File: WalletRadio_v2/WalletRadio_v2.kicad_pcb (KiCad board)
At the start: 2 copper layers, 93.9 x 64 mm, 33 parts, among them Q1 BSP315P, Q2 Q_NPN_ECB, SW1 SW_SPDT, U1 BB201, U2 BB201, U3 LM324A

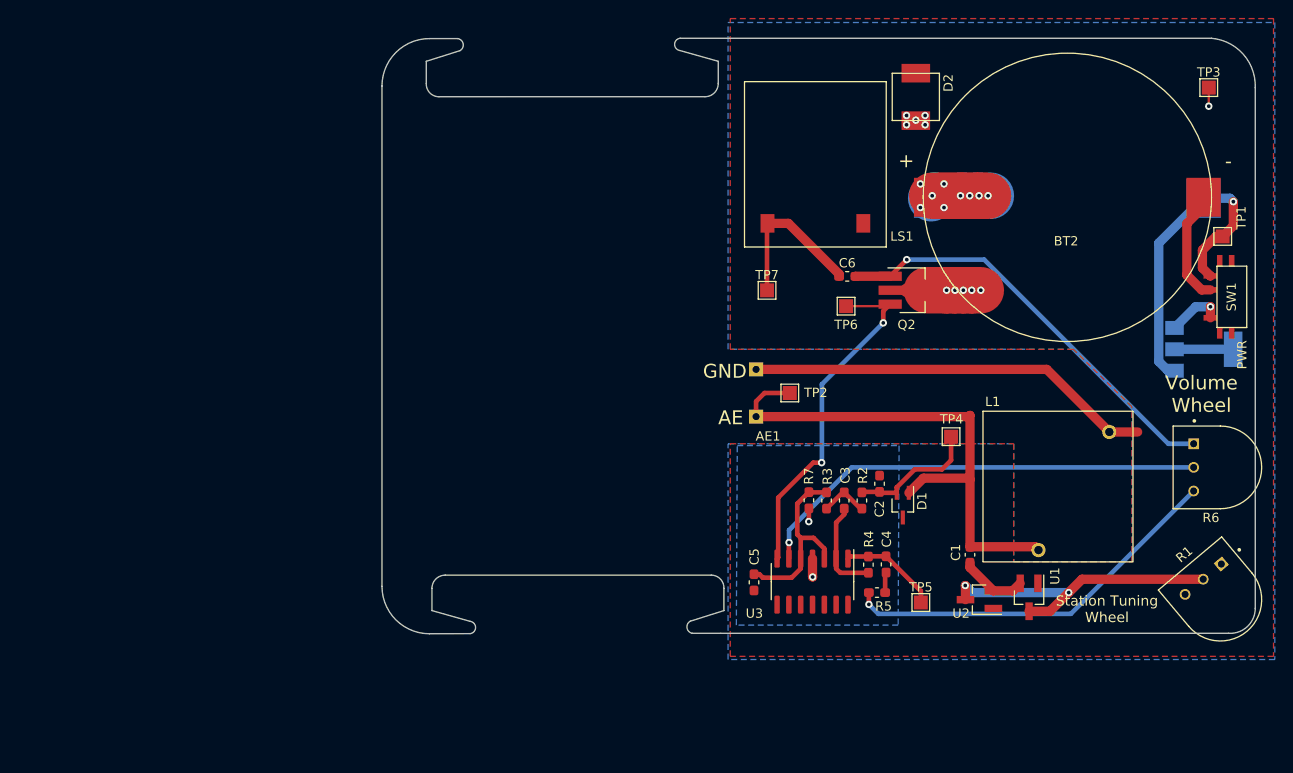
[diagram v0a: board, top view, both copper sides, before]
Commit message: Changed the coin cell holder. Redid entire PCB layout
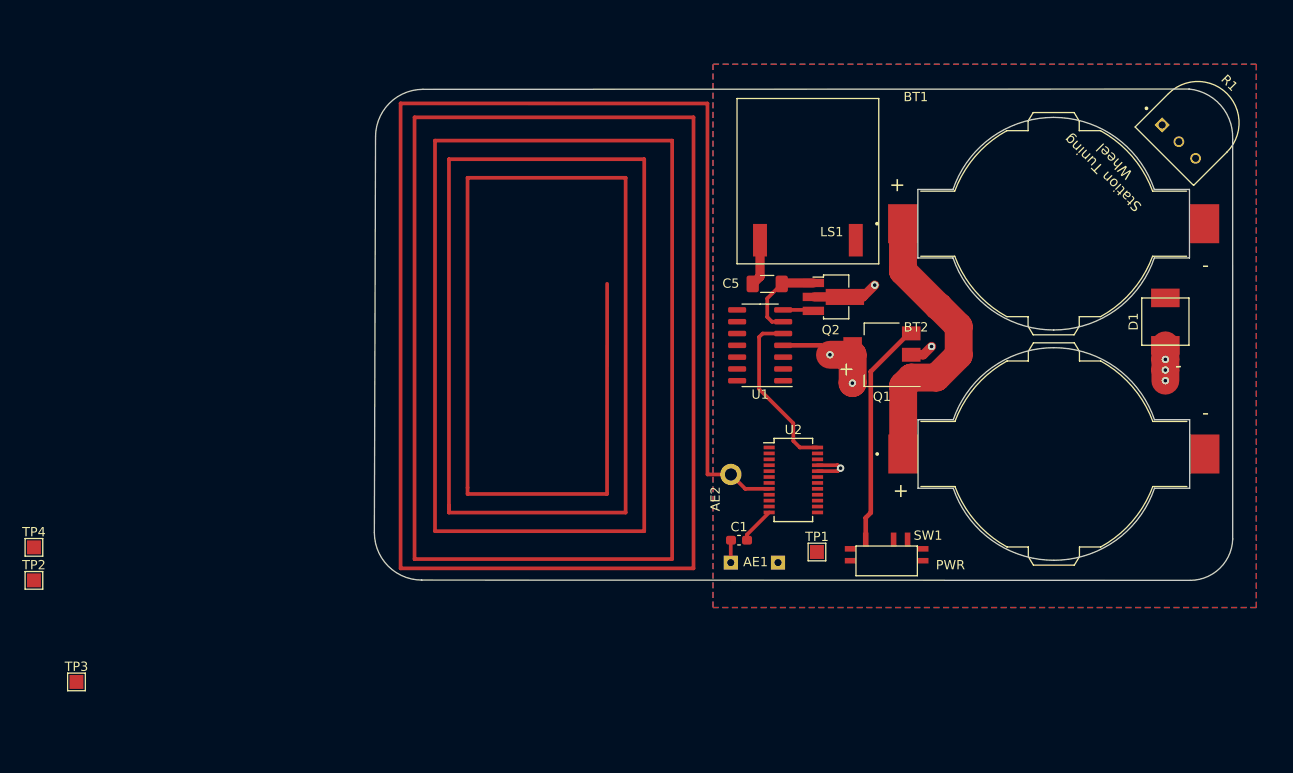
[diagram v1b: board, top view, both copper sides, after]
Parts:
- removed C2: 300pF, Capacitor_SMD:C_0603_1608Metric_Pad1.05x0.95mm_HandSolder
- removed C3: 0.1uF, Capacitor_SMD:C_0603_1608Metric_Pad1.05x0.95mm_HandSolder
- removed C4: 0.47uF, Capacitor_SMD:C_0603_1608Metric_Pad1.05x0.95mm_HandSolder
- removed C6: 100uF, Resistor_SMD:R_0603_1608Metric_Pad1.05x0.95mm_HandSolder
- removed D2: D_TVS, WalletRadio:5.0SMDJ9.0CA
- removed L1: 168uH, WalletRadio:PE-53828NL
- removed R2: 100K, Resistor_SMD:R_0603_1608Metric_Pad1.05x0.95mm_HandSolder
- removed R3: 120K, Resistor_SMD:R_0603_1608Metric_Pad1.05x0.95mm_HandSolder
- removed R4: 1M, Resistor_SMD:R_0603_1608Metric_Pad1.05x0.95mm_HandSolder
- removed R5: 10K, Resistor_SMD:R_0603_1608Metric_Pad1.05x0.95mm_HandSolder
- removed R6: 3352T-1-104LF, WalletRadio:TRIM_3352T-1-103LF
- removed R7: 220K, Resistor_SMD:R_0603_1608Metric_Pad1.05x0.95mm_HandSolder
- removed TP5, TP6, TP7: TestPoint, TestPoint:TestPoint_Pad_1.5x1.5mm
- removed U3: LM324A, Package_SO:SOIC-14_3.9x8.7mm_P1.27mm
- added AE2: Antenna, WalletRadio:FM_antenna, F.Cu at (140.5, 117.8)
- BT1: value Battery_Cell -> BU2032SM-JJ-MINI-GTR; footprint WalletRadio:20mmCoinCell -> WalletRadio:BAT_BU2032SM-JJ-MINI-GTR; moved to F.Cu
- BT2: value Battery_Cell -> BU2032SM-JJ-MINI-GTR; footprint WalletRadio:20mmCoinCell -> WalletRadio:BAT_BU2032SM-JJ-MINI-GTR
- C1: value 10n -> 0.47u
- C5: value 0.1uF -> 100uF; footprint Capacitor_SMD:C_0603_1608Metric_Pad1.05x0.95mm_HandSolder -> Capacitor_SMD:C_1206_3216Metric_Pad1.33x1.80mm_HandSolder
- D1: value 1N34 Germanium Diode -> D_TVS; footprint Package_TO_SOT_SMD:SOT-323_SC-70_Handsoldering -> WalletRadio:5.0SMDJ9.0CA
- Q1: moved to F.Cu
- R1: value 3352T-1-103LF -> 3352T-1-104LF
- U1: value BB201 -> LM324A; footprint Package_TO_SOT_SMD:SOT-23_Handsoldering -> Package_SO:SOIC-14_3.9x8.7mm_P1.27mm
- U2: value BB201 -> Si4824; footprint Package_TO_SOT_SMD:SOT-23_Handsoldering -> Package_SO:SSOP-24_3.9x8.7mm_P0.635mm
- moved TP3 137.5 mm to (71.2, 140.1)
- moved TP4 99.3 mm to (66.7, 125.6)
- moved TP2 83.7 mm to (66.7, 129.2)
- moved TP1 55.3 mm to (150.9, 126.1)
- moved R1 51.3 mm to (191.8, 80.0), turned to -45 degrees
- moved U1 39.6 mm to (144.8, 103.9), turned to 180 degrees
- moved SW1 39.6 mm to (158.4, 122.0), turned to 0 degrees
- moved Q1 34.6 mm to (157.9, 104.9), turned to 180 degrees
- moved D1 34.4 mm to (188.3, 101.3), turned to 90 degrees
- moved C5 32.1 mm to (145.5, 97.3), turned to 0 degrees
- moved BT2 27.6 mm to (176.4, 115.6)
- moved C1 24.9 mm to (142.5, 124.8), turned to 0 degrees
- moved U2 23.8 mm to (148.3, 118.4), turned to 0 degrees
- moved AE1 18.2 mm to (144.1, 127.3), turned to 0 degrees
- moved Q2 8.12 mm to (152.6, 98.7)
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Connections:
- AE1 pad 1: GND -> Net-(AE1-Pad1)
- AE1 pad 2: Net-(AE1-Pad2) -> GND
- C1 pad 1: Net-(AE1-Pad2) -> Net-(AE1-Pad1)
- C5 pad 2: GND -> Net-(C5-Pad2)
- D1 pad 1: Net-(AE1-Pad2) -> /+Vbat
- D1 pad 2: Net-(C2-Pad1) -> GND
- LS1 pad 1: Net-(C6-Pad1) -> Net-(C5-Pad1)
- Q1 pad 1: Net-(BT1-Pad1) -> Net-(BT1-Pad+)
- Q2 pad 1: Net-(C6-Pad2) -> Net-(C5-Pad2)
- R1 pad 1: GND -> /TUNE1
- R1 pad 3: /+Vbat -> GND
- SW1 pad 3: Net-(BT1-Pad1) -> Net-(BT1-Pad+)
- TP1 pad 1: Net-(BT1-Pad1) -> Net-(BT1-Pad+)
- TP2 pad 1: Net-(AE1-Pad2) -> /+Vbat
- TP3 pad 1: /+Vbat -> Net-(Q2-Pad3)
- TP4 pad 1: Net-(C2-Pad1) -> Net-(C5-Pad1)
- U1 pad 1: GND -> (no net)
- U1 pad 2: Net-(C1-Pad2) -> (no net)
- U1 pad 3: Net-(R1-Pad2) -> (no net)
- U2 pad 1: GND -> unconnected-(U2-Pad1)
- U2 pad 2: Net-(C1-Pad2) -> unconnected-(U2-Pad2)
- U2 pad 3: Net-(R1-Pad2) -> /TUNE1
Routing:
- net Net-(AE1-Pad2): track 57.8 -> 0.00 mm
- net GND: track 56.1 -> 0.00 mm
- net Net-(R6-Pad2): track 49.4 -> 0.00 mm, vias 1 -> 0
- net Net-(C6-Pad2): track 45.3 -> 0.00 mm, vias 1 -> 0
- net Net-(R5-Pad1): track 42.1 -> 0.00 mm, vias 1 -> 0
- net Net-(BT1-Pad1): track 35.2 -> 0.00 mm, vias 1 -> 0
- net Net-(Q2-Pad3): track 37.8 -> 3.29 mm, vias 2 -> 0
- net Net-(R1-Pad2): track 33.1 -> 0.00 mm, vias 2 -> 0
- net Net-(BT1-Pad+): track 0.00 -> 31.3 mm
- net Net-(Q1-Pad3): track 5.99 -> 24.3 mm, vias 1 -> 0
- net Net-(C6-Pad1): track 17.4 -> 0.00 mm
- net Net-(C5-Pad1): track 20.5 -> 5.03 mm
- net Net-(C2-Pad1): track 14.0 -> 0.00 mm
- net Net-(BT1-Pad2): track 12.5 -> 0.00 mm, vias 9 -> 0
- net /+Vbat: track 17.5 -> 29.6 mm, vias 13 -> 8
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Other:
- board size 93.9 x 64 mm -> 92.3 x 52.8 mm
- board text removed: "AE"
- board text removed: "GND"
- board text removed: "Volume Wheel"

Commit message: Added the remaining footprints for the components and continued laying out
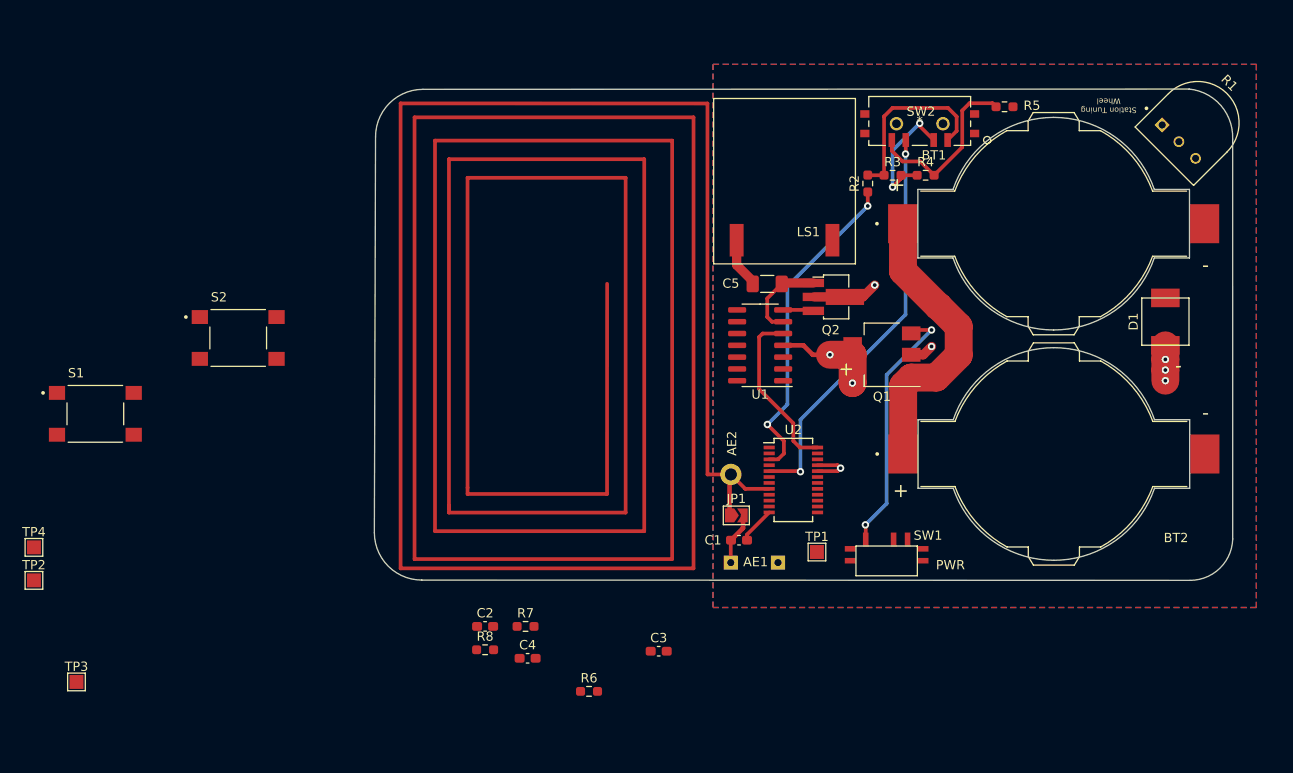
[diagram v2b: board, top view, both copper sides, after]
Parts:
- added C2: 0.1u, Capacitor_SMD:C_0603_1608Metric_Pad1.08x0.95mm_HandSolder, F.Cu at (115.2, 134.1)
- added C3: 0.1u, Capacitor_SMD:C_0603_1608Metric_Pad1.08x0.95mm_HandSolder, F.Cu at (133.9, 136.8)
- added C4: 0.1uF, Capacitor_SMD:C_0603_1608Metric_Pad1.08x0.95mm_HandSolder, F.Cu at (119.8, 137.5)
- added JP1: SolderJumper_2_Open, Jumper:SolderJumper-2_P1.3mm_Open_TrianglePad1.0x1.5mm, F.Cu at (142.2, 122.2)
- added R2: 143k, Resistor_SMD:R_0603_1608Metric_Pad0.98x0.95mm_HandSolder, F.Cu at (156.3, 86.5)
- added R3: 110k, Resistor_SMD:R_0603_1608Metric_Pad0.98x0.95mm_HandSolder, F.Cu at (159.0, 85.6)
- added R4: 180k, Resistor_SMD:R_0603_1608Metric_Pad0.98x0.95mm_HandSolder, F.Cu at (162.6, 85.6)
- added R5: 67k, Resistor_SMD:R_0603_1608Metric_Pad0.98x0.95mm_HandSolder, F.Cu at (171.0, 78.2)
- added R6: 100k, Resistor_SMD:R_0603_1608Metric_Pad0.98x0.95mm_HandSolder, F.Cu at (126.4, 141.1)
- added R7: 56k, Resistor_SMD:R_0603_1608Metric_Pad0.98x0.95mm_HandSolder, F.Cu at (119.5, 134.1)
- added R8: 56k, Resistor_SMD:R_0603_1608Metric_Pad0.98x0.95mm_HandSolder, F.Cu at (115.2, 136.6)
- added S1: TS05-66-43-BK-260-SMT-67, WalletRadio:SW_TS05-66-43-BK-260-SMT-67, F.Cu at (73.3, 111.3)
- added S2: TS05-66-43-BK-260-SMT-67, WalletRadio:SW_TS05-66-43-BK-260-SMT-67, F.Cu at (88.6, 103.1)
- added SW2: CUS-13TB, WalletRadio:CUS-13TB, F.Cu at (161.9, 79.8)
- moved LS1 2.51 mm to (147.4, 92.6)
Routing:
- net Net-(SW2-Pad3): track 0.00 -> 43.7 mm, vias 0 -> 2
- net /TUNE1: track 0.00 -> 35.2 mm, vias 0 -> 2
- net Net-(R2-Pad2): track 0.00 -> 19.6 mm
- net Net-(R4-Pad2): track 0.00 -> 19.1 mm
- net Net-(R3-Pad2): track 0.00 -> 13.9 mm, vias 0 -> 2
- net Net-(AE2-Pad1): track 4.76 -> 9.22 mm
- net Net-(Q1-Pad3): track 24.3 -> 27.8 mm, vias 0 -> 2
- net Net-(AE1-Pad1): track 2.42 -> 5.63 mm

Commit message: Did more layout
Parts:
- R7, R8, S1, S2: moved to B.Cu
- moved S1 83.5 mm to (152.0, 83.4), turned to 90 degrees
- moved S2 58.7 mm to (143.9, 83.3), turned to -90 degrees
- moved R8 55.1 mm to (146.9, 91.5), turned to -90 degrees
- moved R7 49.6 mm to (144.9, 91.5), turned to -90 degrees
- moved C4 47.1 mm to (150.9, 102.2)
- moved C2 43.8 mm to (154.6, 114.9)
- moved R6 37.1 mm to (155.4, 118.0), turned to -90 degrees
- moved C3 25.1 mm to (153.7, 121.4), turned to 90 degrees
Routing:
- net Net-(R1-Pad2): track 0.00 -> 76.5 mm, vias 0 -> 1
- net /TUNE1: track 35.2 -> 78.0 mm
- net /VOL+: track 0.00 -> 42.2 mm, vias 0 -> 1
- net /VOL-: track 0.00 -> 40.7 mm, vias 0 -> 1
- net Net-(BT1-Pad+): track 31.3 -> 53.5 mm, vias 0 -> 2
- net Net-(C3-Pad2): track 0.00 -> 5.21 mm
- net /+Vbat: track 29.6 -> 33.7 mm
- net Net-(C2-Pad1): track 0.00 -> 3.26 mm
- net Net-(C4-Pad1): track 18.3 -> 21.3 mm
- net Net-(Q1-Pad3): track 27.8 -> 28.6 mm
- net GND: vias 0 -> 2

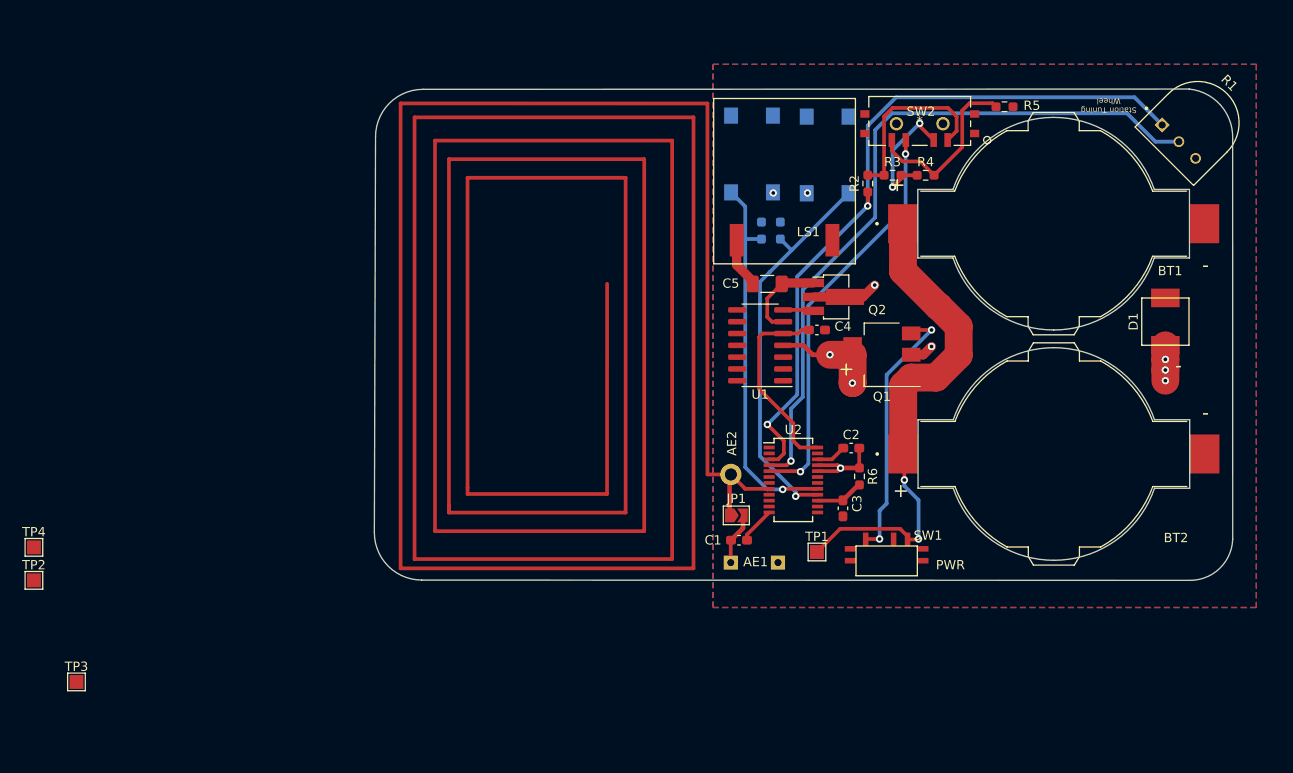
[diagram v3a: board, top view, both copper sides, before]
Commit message: Switched to LiIon battery; rerouted, also added battery charger w/ USB-C
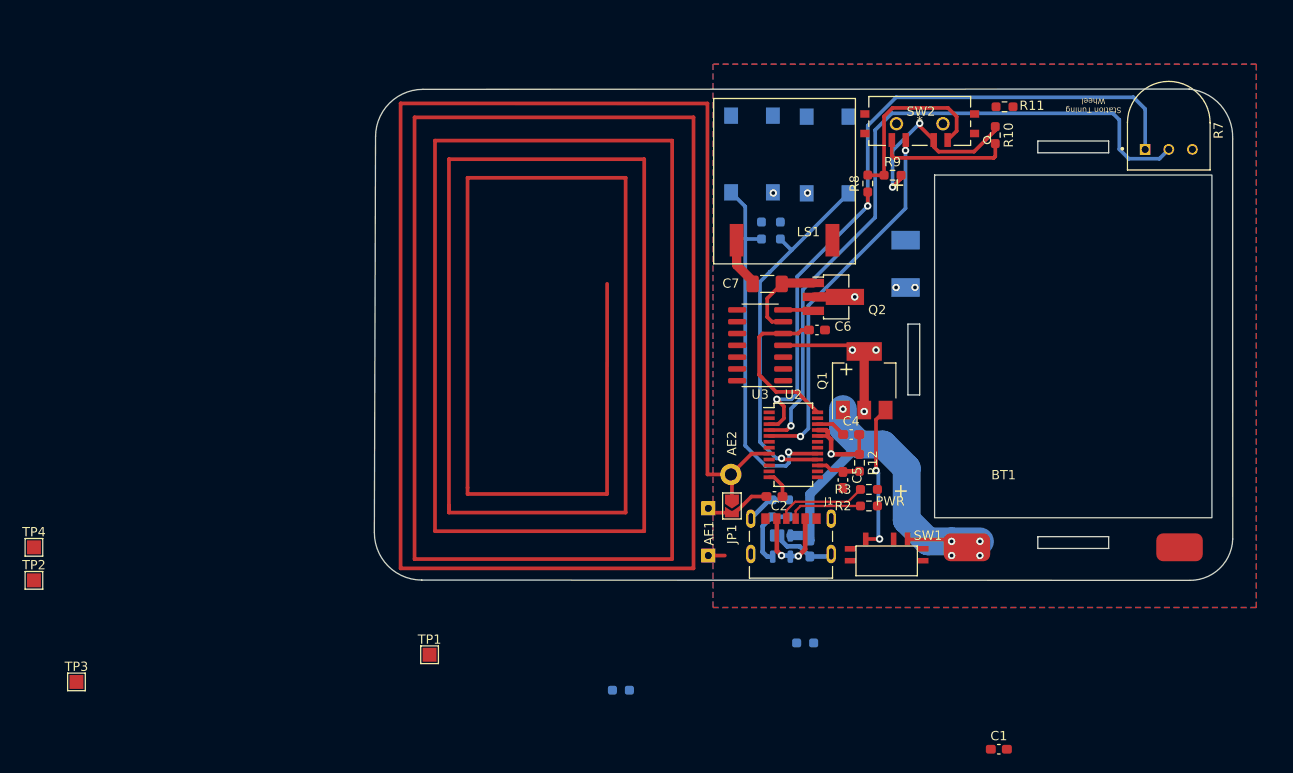
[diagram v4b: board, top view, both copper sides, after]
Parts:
- removed BT2: BU2032SM-JJ-MINI-GTR, WalletRadio:BAT_BU2032SM-JJ-MINI-GTR
- added C1: 4.7u, Capacitor_SMD:C_0603_1608Metric_Pad1.08x0.95mm_HandSolder, F.Cu at (170.4, 147.3)
- added C3: 4.7u, Capacitor_SMD:C_0603_1608Metric_Pad1.08x0.95mm_HandSolder, B.Cu at (150.1, 125.7)
- added J1: UJC-HP-3-SMT-TR, WalletRadio:CUI_UJC-HP-3-SMT-TR, F.Cu at (148.1, 122.5)
- added R1: 330, Resistor_SMD:R_0603_1608Metric_Pad0.98x0.95mm_HandSolder, B.Cu at (129.8, 141.0)
- added R2: 5k, Resistor_SMD:R_0603_1608Metric_Pad0.98x0.95mm_HandSolder, F.Cu at (156.5, 121.2)
- added R3: 5k, Resistor_SMD:R_0603_1608Metric_Pad0.98x0.95mm_HandSolder, F.Cu at (156.5, 119.4)
- added R4: 2k, Resistor_SMD:R_0603_1608Metric_Pad0.98x0.95mm_HandSolder, B.Cu at (147.8, 121.4)
- added R5: 2k, Resistor_SMD:R_0603_1608Metric_Pad0.98x0.95mm_HandSolder, B.Cu at (146.1, 121.4)
- added R6: 330, Resistor_SMD:R_0603_1608Metric_Pad0.98x0.95mm_HandSolder, B.Cu at (149.6, 135.9)
- added U1: MCP73831-2-OT, Package_TO_SOT_SMD:SOT-23-5, B.Cu at (147.1, 125.5)
- BT1: value BU2032SM-JJ-MINI-GTR -> Battery_Cell; footprint WalletRadio:BAT_BU2032SM-JJ-MINI-GTR -> WalletRadio:1578_LiIon_Bat
- D2: renamed from D1; moved to B.Cu
- moved TP1 43.1 mm to (109.2, 137.2)
- moved D2 28.6 mm to (160.4, 95.1), turned to -90 degrees
- moved BT1 13.4 mm to (178.4, 104.0)
- moved R10 8.65 mm to (170.1, 81.3), turned to -90 degrees
- moved C2 6.05 mm to (146.3, 120.1)
- moved AE1 5.95 mm to (139.2, 124.0), turned to -90 degrees
- moved U2 3.78 mm to (148.3, 114.6)
- moved Q1 3.38 mm to (156.0, 107.7), turned to 90 degrees
- moved R7 3.12 mm to (188.7, 79.9), turned to 0 degrees
- moved C5 3.05 mm to (153.7, 118.4)
- moved R12 1.46 mm to (155.4, 116.5)
- moved C4 1.46 mm to (154.6, 113.5)
- moved JP1 1.12 mm to (141.7, 121.2), turned to -90 degrees
- renumbered C1 to C2, C2 to C4, C3 to C5, C4 to C6, C5 to C7, R4 to R10, R5 to R11, R6 to R12, R7 to R13, R8 to R14, R1 to R7, R2 to R8, R3 to R9, U1 to U3
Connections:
- Q1 pad 1: Net-(BT1-Pad+) -> /raw_Vbat
- SW1 pad 3: Net-(BT1-Pad+) -> /raw_Vbat
- TP1 pad 1: Net-(BT1-Pad+) -> /raw_Vbat
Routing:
- net Net-(BT1-Pad+): track 53.5 -> 0.00 mm, vias 2 -> 0
- net /raw_Vbat: track 0.00 -> 48.4 mm, vias 0 -> 5
- net GND: track 0.00 -> 13.4 mm, vias 2 -> 4
- net Net-(Q1-Pad3): track 28.6 -> 16.0 mm
- net Net-(C1-Pad2): track 0.00 -> 10.4 mm, vias 0 -> 2
- net Net-(J1-PadA5): track 0.00 -> 9.77 mm
- net Net-(J1-PadB5): track 0.00 -> 8.02 mm
- net Net-(R4-Pad1): track 0.00 -> 7.28 mm
- net Net-(R10-Pad1): track 13.9 -> 21.1 mm
- net /+Vbat: track 33.7 -> 28.7 mm, vias 8 -> 5
- net Net-(R10-Pad2): track 19.1 -> 14.3 mm
- net Net-(SW2-Pad3): track 43.7 -> 40.0 mm
- net Net-(C6-Pad1): track 21.3 -> 18.1 mm
- net /VOL+: track 42.2 -> 39.4 mm
- net /TUNE1: track 78.0 -> 76.1 mm
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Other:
- outline, holes or cut-outs redrawn
- board text removed: "-"

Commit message: Did more PCB layout.
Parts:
- removed the R5 at (146.1, 121.4)
- added D1: LED, LED_SMD:LED_0603_1608Metric_Pad1.05x0.95mm_HandSolder, F.Cu at (161.0, 120.8)
- added D3: LED, LED_SMD:LED_0603_1608Metric_Pad1.05x0.95mm_HandSolder, B.Cu at (154.9, 126.5)
- added D4: KDZVTFTR3.3B, WalletRadio:KDZVTFTR3.3B, F.Cu at (157.7, 99.1)
- R1: moved to F.Cu
- moved R1 39.5 mm to (161.0, 116.8), turned to -90 degrees
- moved C1 29.0 mm to (154.4, 123.2), turned to 90 degrees
- moved R7 14.0 mm to (154.9, 122.9), turned to -90 degrees
- moved R3 1.70 mm to (157.2, 122.7)
- moved R4 1.70 mm to (157.2, 120.9)
- moved R5 1.08 mm to (147.1, 122.2), turned to 0 degrees
- renumbered R9 to R10, R10 to R11, R11 to R12, R12 to R13, R13 to R14, R14 to R15, R2 to R3, R3 to R4, R4 to R5, R6 to R7, R7 to R8, R8 to R9
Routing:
- net Net-(D3-Pad1): track 0.00 -> 23.1 mm, vias 0 -> 2
- net /+Vbat: track 28.7 -> 44.4 mm
- net Net-(C1-Pad2): track 10.4 -> 25.7 mm, vias 2 -> 3
- net GND: track 13.4 -> 20.4 mm
- net Net-(D1-Pad2): track 0.00 -> 2.16 mm
- net Net-(J1-PadB5): track 8.02 -> 9.88 mm
- net Net-(D3-Pad2): track 0.00 -> 1.77 mm
- net Net-(R5-Pad1): track 7.28 -> 6.20 mm
- net Net-(J1-PadA5): track 9.77 -> 10.5 mm

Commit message: more layout
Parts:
- moved R13 1.65 mm to (154.7, 115.1), turned to 0 degrees
- moved C5 0.92 mm to (153.2, 117.6)
- moved C6 0.38 mm to (150.9, 102.6)
- moved C4 0.13 mm to (154.7, 113.4)
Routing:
- net GND: track 20.4 -> 17.2 mm
- net Net-(C5-Pad2): track 4.83 -> 5.89 mm
- net /+Vbat: track 44.4 -> 43.4 mm
- added copper zone on F.Cu, net /+Vbat
